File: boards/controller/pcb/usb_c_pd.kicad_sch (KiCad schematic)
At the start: 15 parts, among them J5001 699C124-2A6-111, U5001 USBLC6-2SC6, U5002 TCPP01-M12, U5003 ISZ065N03L5SATMA1

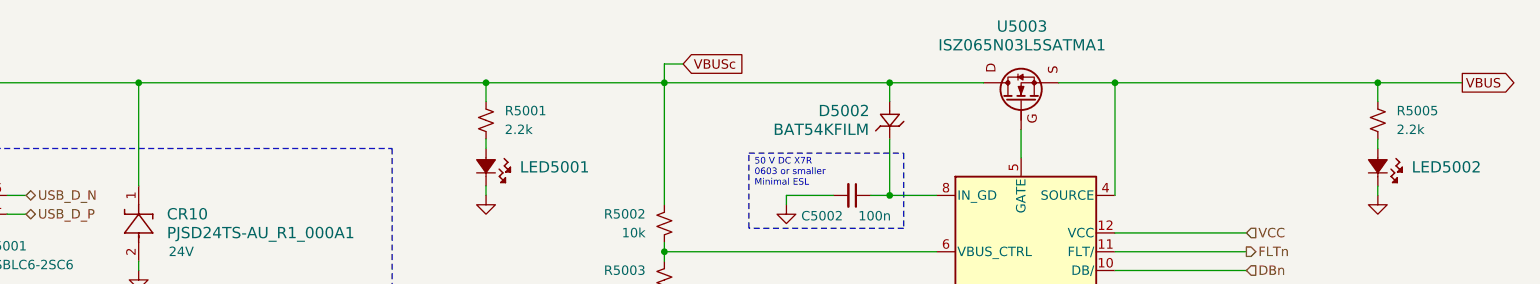
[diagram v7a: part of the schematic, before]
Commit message: controller: pcb: Update schematic
Signed-off-by: Nicholas Loehrke <nicholasnloehrke@gmail.com>
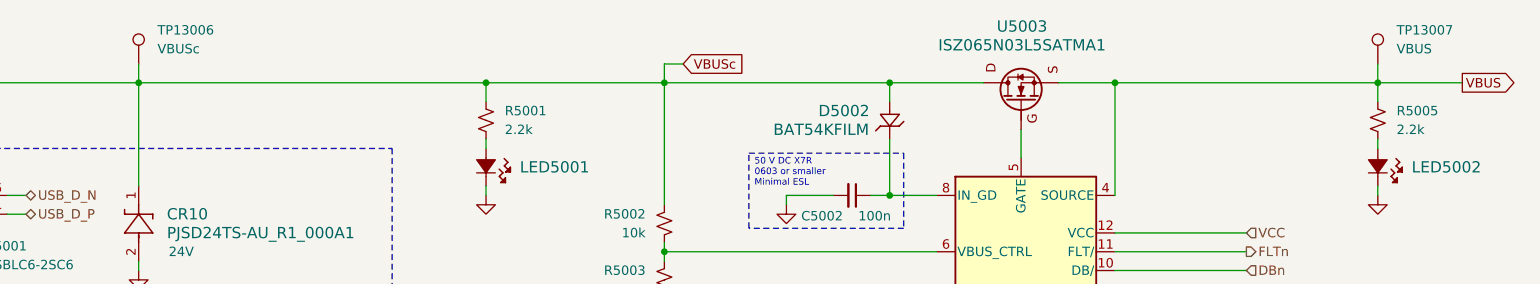
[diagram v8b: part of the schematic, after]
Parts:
- added TP13006: VBUSc, symbol Connector:TestPoint
- added TP13007: VBUS, symbol Connector:TestPoint
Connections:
- net VBUS: now also TP13007.1
- net VBUSc: now also TP13006.1
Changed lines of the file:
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@@
+	(wire
+		(pts
+			(xy 250.19 71.12) (xy 250.19 73.66)
+		)
+		(stroke
+			(width 0)
+			(type default)
+		)
+	)
 	(wire
 		(pts
@@
 		(pts
 			(xy 153.67 96.52) (xy 190.5 96.52)
+		)
+		(stroke
+			(width 0)
+			(type default)
+		)
+	)
+	(wire
+		(pts
+			(xy 82.55 71.12) (xy 82.55 73.66)
 		)
 		(stroke
@@
 	)
 	(symbol
+		(lib_id "Connector:TestPoint")
+		(at 250.19 71.12 0)
+		(unit 1)
+		(exclude_from_sim no)
+		(in_bom yes)
+		(on_board yes)
+		(dnp no)
+		(fields_autoplaced yes)
+		(property "Reference" "TP13007"
+			(at 252.73 66.5479 0)
+			(effects
+				(font
+					(size 1.27 1.27)
+				)
+				(justify left)
+			)
+		)
+		(property "Value" "VBUS"
+			(at 252.73 69.0879 0)
+			(effects
+				(font
+					(size 1.27 1.27)
+				)
+				(justify left)
+			)
+		)
+		(property "Footprint" ""
+			(at 255.27 71.12 0)
+			(effects
+				(font
+					(size 1.27 1.27)
+				)
+				(hide yes)
+			)
+		)
+		(property "Datasheet" "~"
+			(at 255.27 71.12 0)
+			(effects
+				(font
+					(size 1.27 1.27)
+				)
+				(hide yes)
+			)
+		)
+		(property "Description" "test point"
+			(at 250.19 71.12 0)
+			(effects
+				(font
+					(size 1.27 1.27)
+				)
+				(hide yes)
+			)
+		)
+		(pin "1"
+		)
+		(instances
+			(project "controller"
+				(path "/5caba13a-97ae-46d4-856f-900b12012fd8/36295df0-8e81-41b3-8cd3-2cdd8b56207c"
+					(reference "TP13007")
+					(unit 1)
+				)
+			)
+		)
+	)
+	(symbol
 		(lib_id "Device:R_Small_US")
 		(at 129.54 78.74 0)
@@
 					(unit 1)
 				)
+			)
+		)
+	)
+	(symbol
+		(lib_id "Connector:TestPoint")
+		(at 82.55 71.12 0)
+		(unit 1)
+		(exclude_from_sim no)
+		(in_bom yes)
+		(on_board yes)
+		(dnp no)
+		(fields_autoplaced yes)
+		(property "Reference" "TP13006"
+			(at 85.09 66.5479 0)
+			(effects
+				(font
+					(size 1.27 1.27)
+				)
+				(justify left)
+			)
+		)
+		(property "Value" "VBUSc"
+			(at 85.09 69.0879 0)
+			(effects
+				(font
+					(size 1.27 1.27)
+				)
+				(justify left)
+			)
+		)
+		(property "Footprint" ""
+			(at 87.63 71.12 0)
+			(effects
+				(font
+					(size 1.27 1.27)
+				)
+				(hide yes)
+			)
+		)
+		(property "Datasheet" "~"
+			(at 87.63 71.12 0)
+			(effects
+				(font
+					(size 1.27 1.27)
+				)
+				(hide yes)
+			)
+		)
+		(property "Description" "test point"
+			(at 82.55 71.12 0)
+			(effects
+				(font
+					(size 1.27 1.27)
+				)
+				(hide yes)
+			)
+		)
+		(pin "1"
+		)
+		(instances
+			(project "controller"
+				(path "/5caba13a-97ae-46d4-856f-900b12012fd8/36295df0-8e81-41b3-8cd3-2cdd8b56207c"
+					(reference "TP13006")
+					(unit 1)
+				)
